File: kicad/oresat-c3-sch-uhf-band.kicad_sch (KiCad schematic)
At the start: 126 parts, among them Q3 NTR4101, Q4 PMV45EN, U16 AX5043, U18 LT5534, U19 BDCN-20-13+, U20 QPC1022, U21 TQP7M9105, U22 LT5534, U25 SN74LVC1G11IDCKRQ1, U26 TLV7041DBV, U27 LP2985AIM5-1.8_NOPB, U29 TQP3M9036, U32 SF2446E, U33 SF2446E, U40 MAX941EUA+, X1 TYKTBLSANF-16.000000

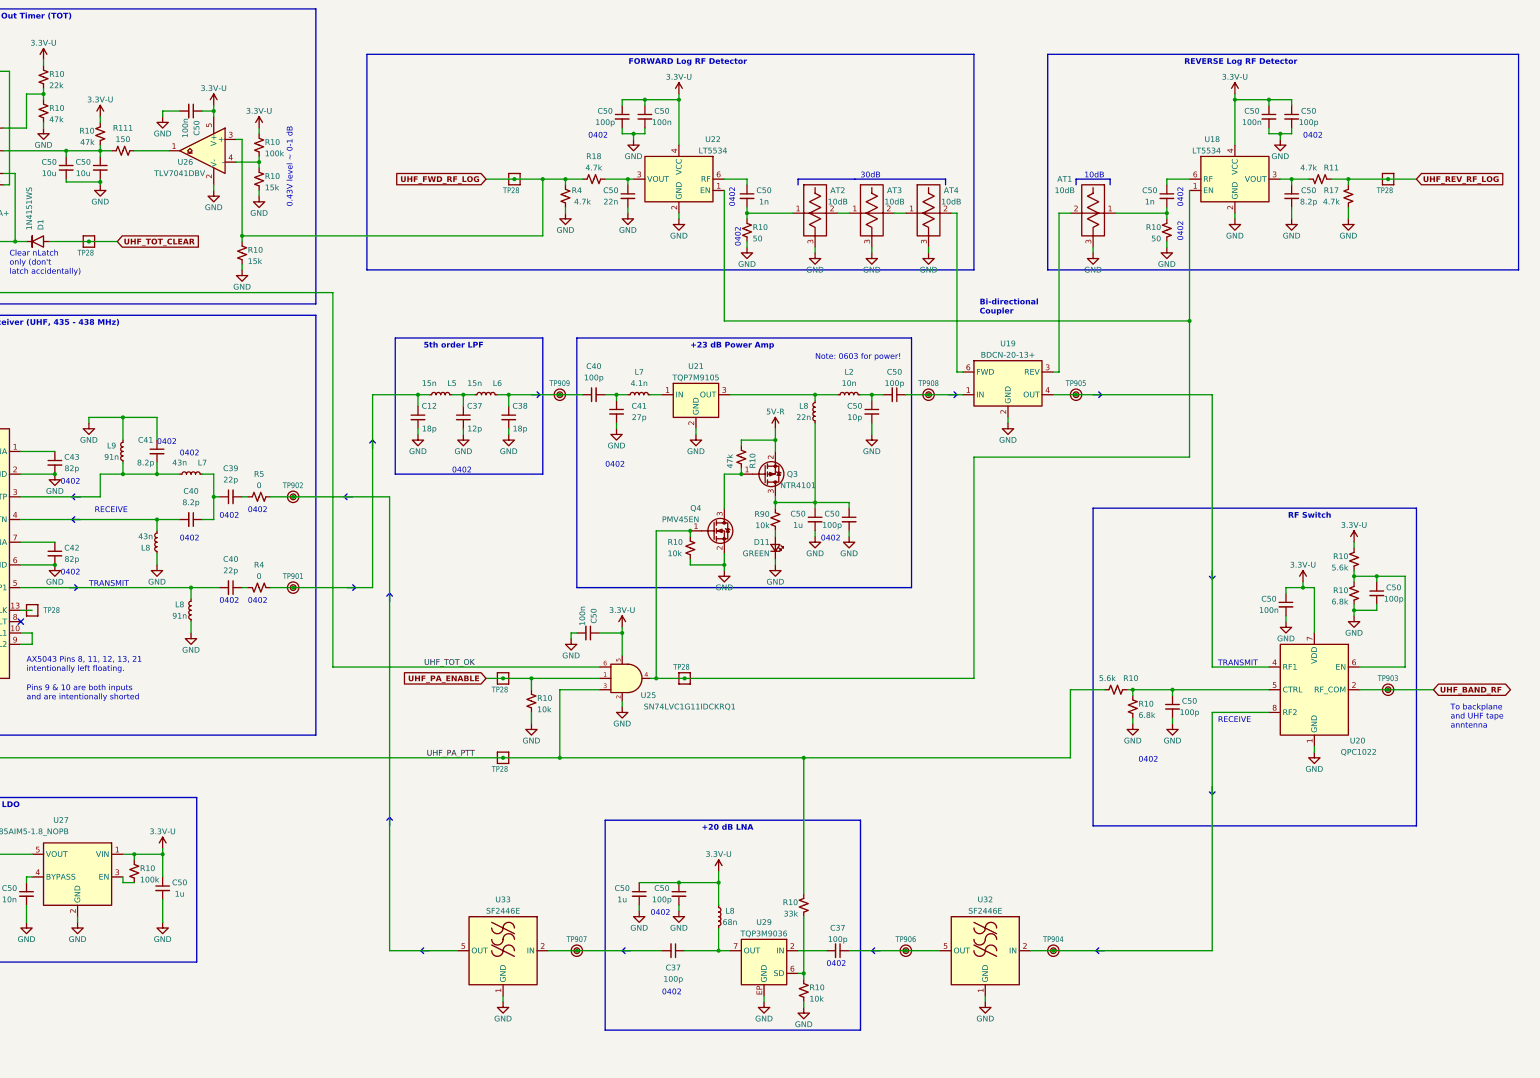
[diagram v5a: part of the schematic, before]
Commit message: Add expected dBm values on radio TX and RXs.
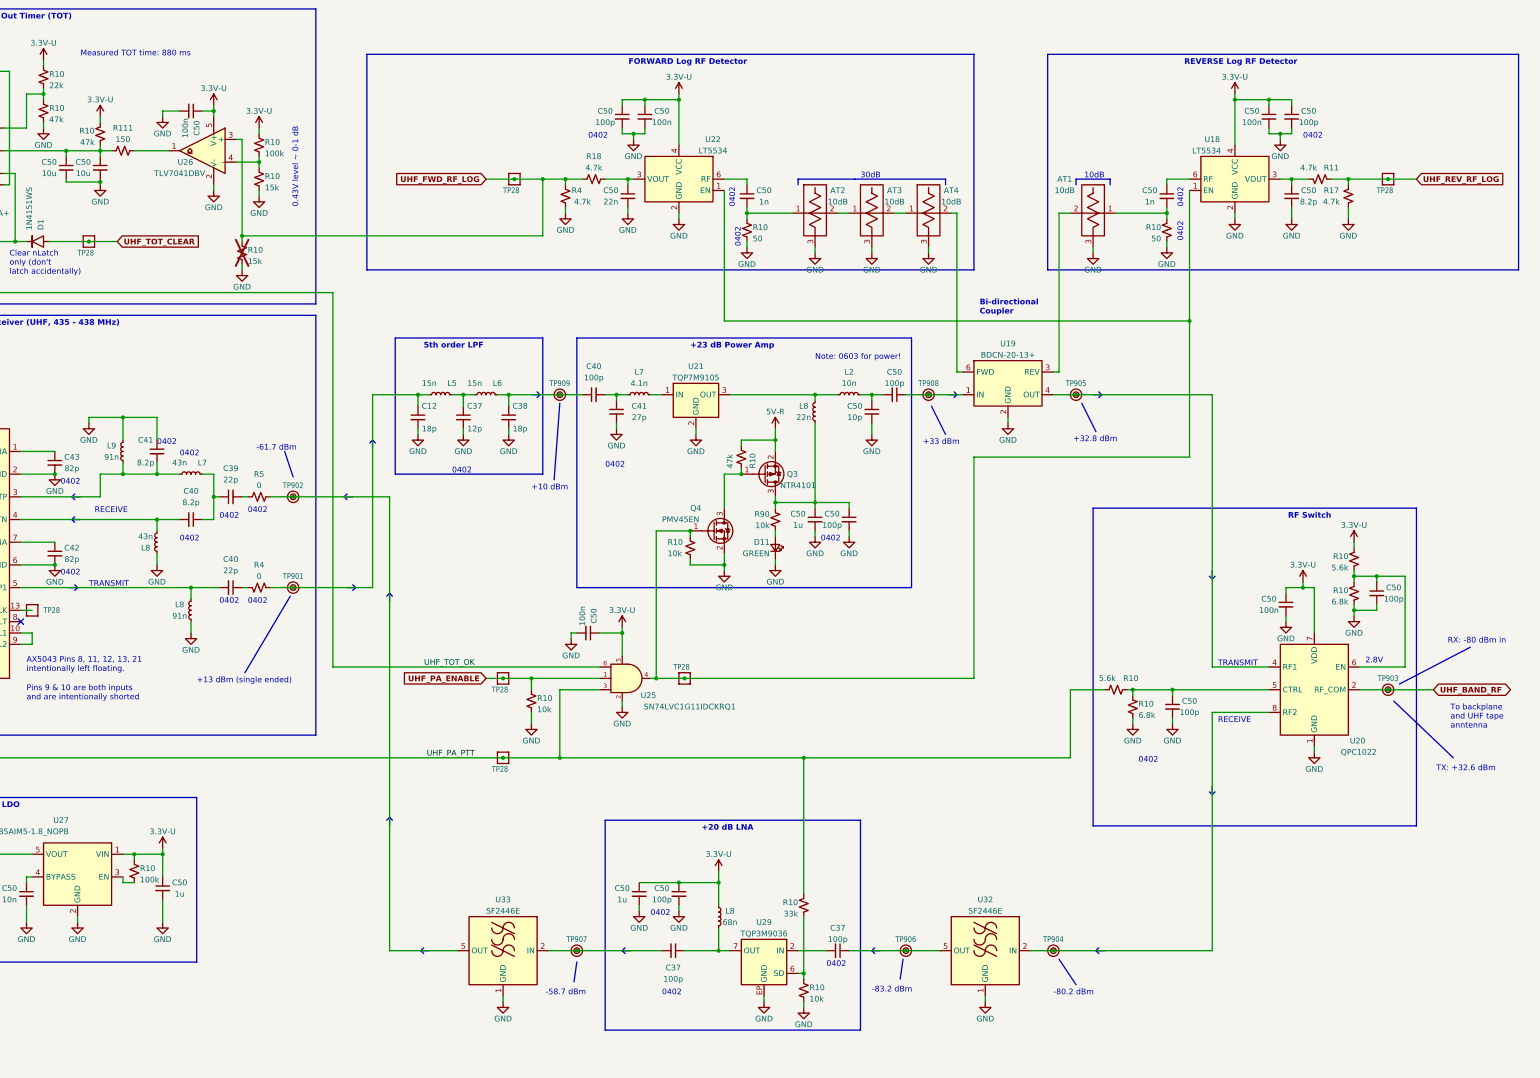
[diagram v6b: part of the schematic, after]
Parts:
- R10: now not fitted
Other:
- note added: "+10 dBm"
- note added: "+13 dBm (single ended)"
- note added: "+32.8 dBm"
- note added: "+33 dBm"
- note added: "-58.7 dBm"
- note added: "-61.7 dBm"
- note added: "-80.2 dBm"
- note added: "-83.2 dBm"
- note added: "2.8V"
- note added: "Measured TOT time: 880 ms"
- note added: "RX: -80 dBm in"
- note added: "TX: +32.6 dBm"
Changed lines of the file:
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@@
     (stroke (width 0) (type default))
   )
+  (polyline (pts (xy 403.225 158.115) (xy 387.35 166.37))
+    (stroke (width 0) (type default))
+  )
   (wire (pts (xy 177.8 109.22) (xy 177.8 110.49))
     (stroke (width 0) (type default))
@@
     (stroke (width 0) (type default))
   )
+  (polyline (pts (xy 198.12 120.65) (xy 199.39 103.505))
+    (stroke (width 0) (type default))
+  )
   (polyline (pts (xy 213.36 226.06) (xy 213.995 226.695))
     (stroke (width 0.254) (type default) (color 146 146 146 1))
@@
     (stroke (width 0) (type default))
   )
+  (polyline (pts (xy 319.405 109.855) (xy 316.23 103.505))
+    (stroke (width 0) (type default))
+  )
   (wire (pts (xy 193.04 172.72) (xy 193.04 175.26))
     (stroke (width 0) (type default))
@@
     (stroke (width 0) (type default))
   )
+  (polyline (pts (xy 202.565 233.045) (xy 203.2 228.6))
+    (stroke (width 0) (type default))
+  )
   (polyline (pts (xy 161.29 196.215) (xy 160.655 196.85))
     (stroke (width 0.254) (type default) (color 146 146 146 1))
@@
     (stroke (width 0) (type default))
   )
+  (polyline (pts (xy 139.7 120.015) (xy 137.795 114.3))
+    (stroke (width 0) (type default))
+  )
   (wire (pts (xy 177.8 101.6) (xy 175.26 101.6))
     (stroke (width 0) (type default))
@@
     (stroke (width 0) (type default))
   )
+  (polyline (pts (xy 399.415 182.88) (xy 386.08 170.18))
+    (stroke (width 0) (type default))
+  )
   (wire (pts (xy 110.49 203.2) (xy 110.49 204.47))
     (stroke (width 0) (type default))
@@
     (stroke (width 0) (type default))
   )
+  (polyline (pts (xy 314.96 233.68) (xy 311.15 227.965))
+    (stroke (width 0) (type default))
+  )
   (polyline (pts (xy 90.17 124.46) (xy 92.075 124.46))
     (stroke (width 0.254) (type default) (color 146 146 146 1))
@@
     (stroke (width 0) (type default))
   )
+  (polyline (pts (xy 275.59 232.41) (xy 276.225 227.965))
+    (stroke (width 0) (type default))
+  )
   (wire (pts (xy 289.56 96.52) (xy 288.29 96.52))
     (stroke (width 0) (type default))
@@
     (stroke (width 0) (type default))
   )
+  (polyline (pts (xy 285.75 110.49) (xy 282.575 104.14))
+    (stroke (width 0) (type default))
+  )
   (wire (pts (xy 48.26 114.3) (xy 38.1 114.3))
     (stroke (width 0) (type default))
@@
     (stroke (width 0) (type default))
   )
+  (polyline (pts (xy 128.905 163.83) (xy 139.065 146.685))
+    (stroke (width 0) (type default))
+  )
   (wire (pts (xy 48.26 127) (xy 38.1 127))
     (stroke (width 0) (type default))
@@
     (effects (font (size 1.27 1.27) (thickness 0.254) bold) (justify left bottom))
   )
+  (text "2.8V" (at 379.73 161.925 0)
+    (effects (font (size 1.27 1.27)) (justify left bottom))
+  )
   (text "0402" (at 114.3 134.62 0)
     (effects (font (size 1.27 1.27)) (justify left bottom))
@@
     (effects (font (size 1.27 1.27)) (justify left bottom))
   )
+  (text "-80.2 dBm" (at 309.88 236.22 0)
+    (effects (font (size 1.27 1.27)) (justify left bottom))
+  )
   (text "0402" (at 219.71 218.44 0)
     (effects (font (size 1.27 1.27)) (justify left bottom))
@@
     (effects (font (size 1.27 1.27)) (justify left bottom))
   )
+  (text "-83.2 dBm" (at 269.24 235.585 0)
+    (effects (font (size 1.27 1.27)) (justify left bottom))
+  )
   (text "+20 dB LNA" (at 231.14 199.39 0)
     (effects (font (size 1.27 1.27) (thickness 0.254) bold) (justify left bottom))
@@
     (effects (font (size 1.27 1.27)) (justify left bottom))
   )
+  (text "+10 dBm" (at 193.04 123.19 0)
+    (effects (font (size 1.27 1.27)) (justify left bottom))
+  )
+  (text "+32.8 dBm" (at 314.325 112.395 0)
+    (effects (font (size 1.27 1.27)) (justify left bottom))
+  )
+  (text "+33 dBm" (at 280.67 113.03 0)
+    (effects (font (size 1.27 1.27)) (justify left bottom))
+  )
   (text "RECEIVE" (at 346.71 175.26 0)
     (effects (font (size 1.27 1.27)) (justify left bottom))
   )
+  (text "RX: -80 dBm in\n" (at 398.145 157.48 0)
+    (effects (font (size 1.27 1.27)) (justify left bottom))
+  )
   (text "0402" (at 123.19 148.59 0)
     (effects (font (size 1.27 1.27)) (justify left bottom))
@@
     (effects (font (size 1.27 1.27)) (justify right bottom))
   )
+  (text "-58.7 dBm" (at 196.215 236.22 0)
+    (effects (font (size 1.27 1.27)) (justify left bottom))
+  )
   (text "Note: 0603 for power!" (at 256.54 93.98 0)
     (effects (font (size 1.27 1.27)) (justify left bottom))
   )
+  (text "Measured TOT time: 880 ms" (at 92.075 26.035 0)
+    (effects (font (size 1.27 1.27)) (justify left bottom))
+  )
   (text "0402" (at 365.76 44.45 0)
     (effects (font (size 1.27 1.27)) (justify left bottom))
@@
     (effects (font (size 1.27 1.27)) (justify left bottom))
   )
+  (text "-61.7 dBm" (at 131.445 114.3 0)
+    (effects (font (size 1.27 1.27)) (justify left bottom))
+  )
   (text "0402" (at 238.76 59.69 90)
     (effects (font (size 1.27 1.27)) (justify left bottom))
@@
     (effects (font (size 1.27 1.27) (thickness 0.254) bold) (justify left bottom))
   )
+  (text "+13 dBm (single ended)" (at 118.11 166.37 0)
+    (effects (font (size 1.27 1.27)) (justify left bottom))
+  )
   (text "0402" (at 129.54 148.59 0)
     (effects (font (size 1.27 1.27)) (justify left bottom))
@@
     (effects (font (size 1.27 1.27) (thickness 0.254) bold) (justify right bottom))
   )
-  (text "0.43V level ~ 0-1 dB" (at 139.7 59.69 90)
+  (text "0.43V level ~ 0-1 dB" (at 140.97 59.69 90)
     (effects (font (size 1.27 1.27)) (justify left bottom))
   )
@@
     (effects (font (size 1.27 1.27)) (justify left bottom))
   )
+  (text "TX: +32.6 dBm" (at 395.605 186.055 0)
+    (effects (font (size 1.27 1.27)) (justify left bottom))
+  )
   (text "0402" (at 175.26 119.38 0)
     (effects (font (size 1.27 1.27)) (justify left bottom))
@@
   )
   (symbol (lib_id "Device:R_Small_US") (at 128.27 69.85 0) (unit 1)
-    (in_bom yes) (on_board yes) (dnp no)
+    (in_bom yes) (on_board yes) (dnp yes)
     (property "Reference" "R10" (at 129.54 69.215 0)
       (effects (font (size 1.27 1.27)) (justify left))

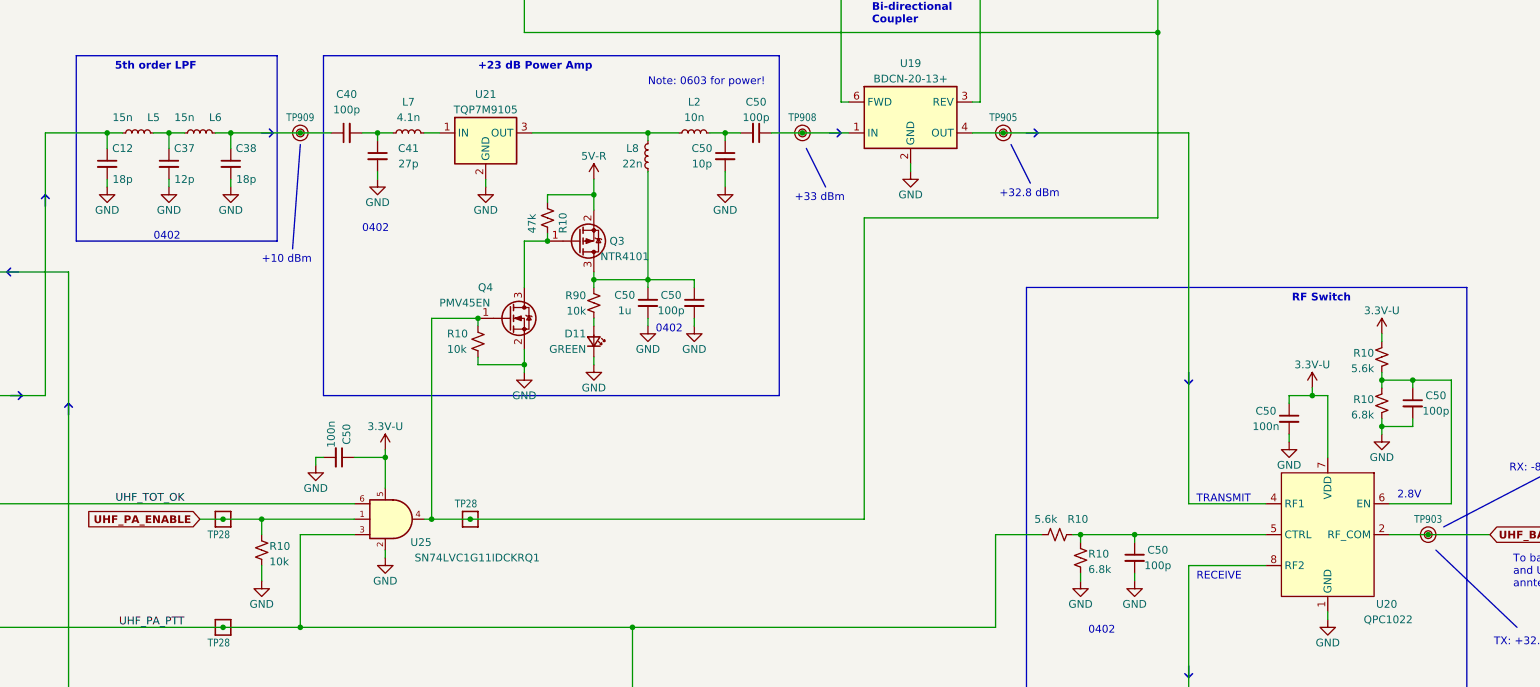
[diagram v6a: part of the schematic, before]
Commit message: changed R values, connected radio enables, more 6.1 implementations
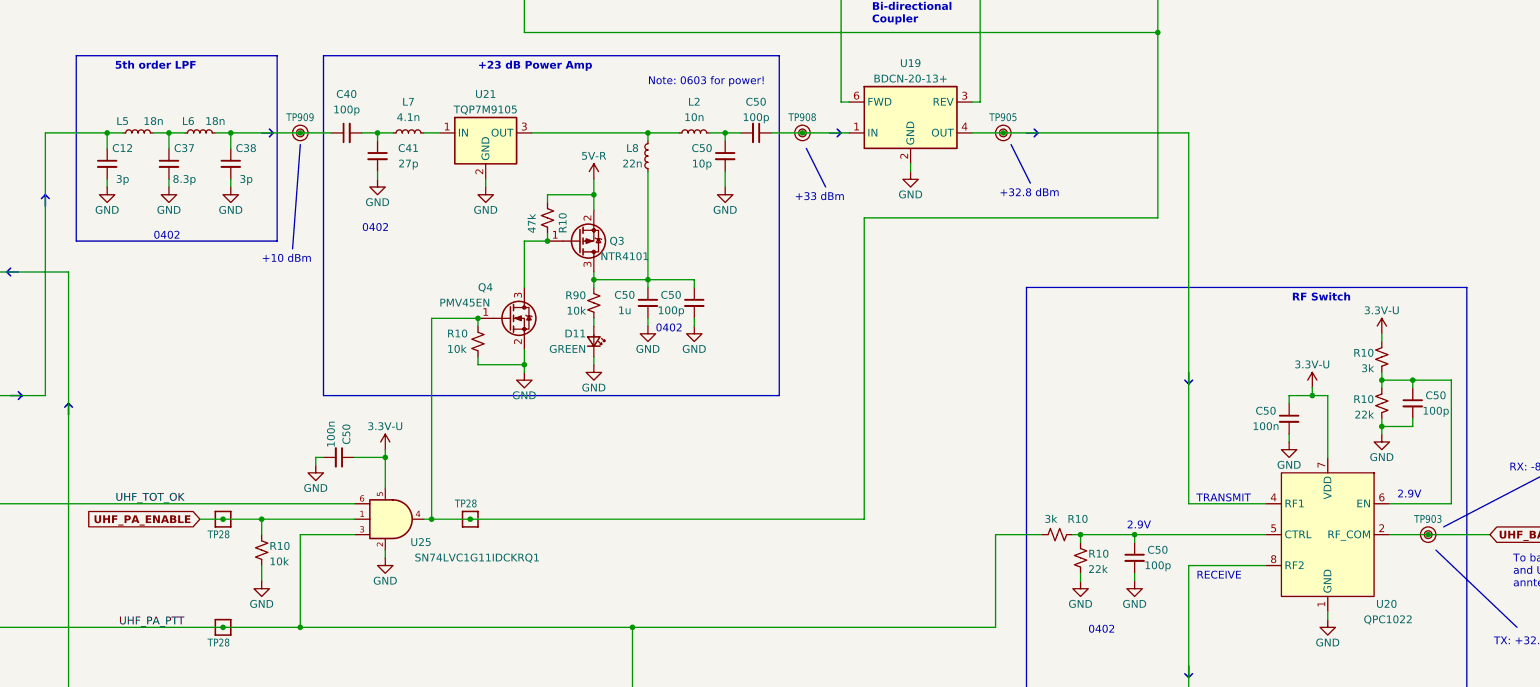
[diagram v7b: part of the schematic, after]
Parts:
- C12, C38: value 18p -> 3p
- C37: value 12p -> 8.3p
- L5, L6: value 15n -> 18n
- R10: value 6.8k -> 22k
- R10: value 5.6k -> 3k
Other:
- note added: "2.9V"
- note removed: "2.8V"
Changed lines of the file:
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@@
     (title "OreSat C3: UHF Band Radio")
     (date "2023-05-29")
-    (rev "6.0")
+    (rev "6.1")
   )
   (junction (at 213.36 154.94) (diameter 0) (color 0 0 0 0)
@@
     (effects (font (size 1.27 1.27) (thickness 0.254) bold) (justify left bottom))
   )
-  (text "2.8V" (at 379.73 161.925 0)
+  (text "2.9V" (at 379.73 161.925 0)
     (effects (font (size 1.27 1.27)) (justify left bottom))
   )
@@
     (effects (font (size 1.27 1.27)) (justify left bottom))
   )
+  (text "2.9V" (at 335.28 167.005 0)
+    (effects (font (size 1.27 1.27)) (justify left bottom))
+  )
   (text "Note: 0603 for power!" (at 256.54 93.98 0)
     (effects (font (size 1.27 1.27)) (justify left bottom))
@@
       (effects (font (size 1.27 1.27)))
     )
-    (property "Value" "12p" (at 180.34 109.22 0)
+    (property "Value" "8.3p" (at 180.34 109.22 0)
       (effects (font (size 1.27 1.27)))
     )
@@
       (effects (font (size 1.27 1.27)))
     )
-    (property "Value" "18p" (at 190.5 109.22 0)
+    (property "Value" "3p" (at 190.5 109.22 0)
       (effects (font (size 1.27 1.27)))
     )
@@
       (effects (font (size 1.27 1.27)) (justify left))
     )
-    (property "Value" "6.8k" (at 328.93 173.355 0)
+    (property "Value" "22k" (at 328.93 173.355 0)
       (effects (font (size 1.27 1.27)) (justify left))
     )
@@
       (effects (font (size 1.27 1.27)) (justify left))
     )
-    (property "Value" "6.8k" (at 375.92 147.955 0)
+    (property "Value" "22k" (at 375.92 147.955 0)
       (effects (font (size 1.27 1.27)) (justify left))
     )
@@
   (symbol (lib_id "Device:L_Small") (at 182.88 101.6 270) (mirror x) (unit 1)
     (in_bom yes) (on_board yes) (dnp no)
-    (property "Reference" "L6" (at 185.42 99.06 90)
+    (property "Reference" "L6" (at 180.975 99.695 90)
       (effects (font (size 1.27 1.27)))
     )
-    (property "Value" "15n" (at 180.34 99.06 90)
+    (property "Value" "18n" (at 185.42 99.695 90)
       (effects (font (size 1.27 1.27)))
     )
@@
   (symbol (lib_id "Device:L_Small") (at 172.72 101.6 270) (mirror x) (unit 1)
     (in_bom yes) (on_board yes) (dnp no)
-    (property "Reference" "L5" (at 175.26 99.06 90)
+    (property "Reference" "L5" (at 170.18 99.695 90)
       (effects (font (size 1.27 1.27)))
     )
-    (property "Value" "15n" (at 170.18 99.06 90)
+    (property "Value" "18n" (at 175.26 99.695 90)
       (effects (font (size 1.27 1.27)))
     )
@@
       (effects (font (size 1.27 1.27)) (justify left))
     )
-    (property "Value" "5.6k" (at 323.85 165.1 90)
+    (property "Value" "3k" (at 323.85 165.1 90)
       (effects (font (size 1.27 1.27)) (justify left))
     )
@@
       (effects (font (size 1.27 1.27)))
     )
-    (property "Value" "18p" (at 170.18 109.22 0)
+    (property "Value" "3p" (at 170.18 109.22 0)
       (effects (font (size 1.27 1.27)))
     )
@@
       (effects (font (size 1.27 1.27)) (justify left))
     )
-    (property "Value" "5.6k" (at 375.92 140.335 0)
+    (property "Value" "3k" (at 375.92 140.335 0)
       (effects (font (size 1.27 1.27)) (justify left))
     )
